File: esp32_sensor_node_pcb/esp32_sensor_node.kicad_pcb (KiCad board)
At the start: 4 copper layers, 49.9 x 59.9 mm, 28 parts, among them J1 Conn_02x10_Odd_Even, Q1 2N7002K, SW1 SW_DIP_x01, U1 HT7833, U2 ESP32-WROOM-E, U3 MAX3483AEASA+

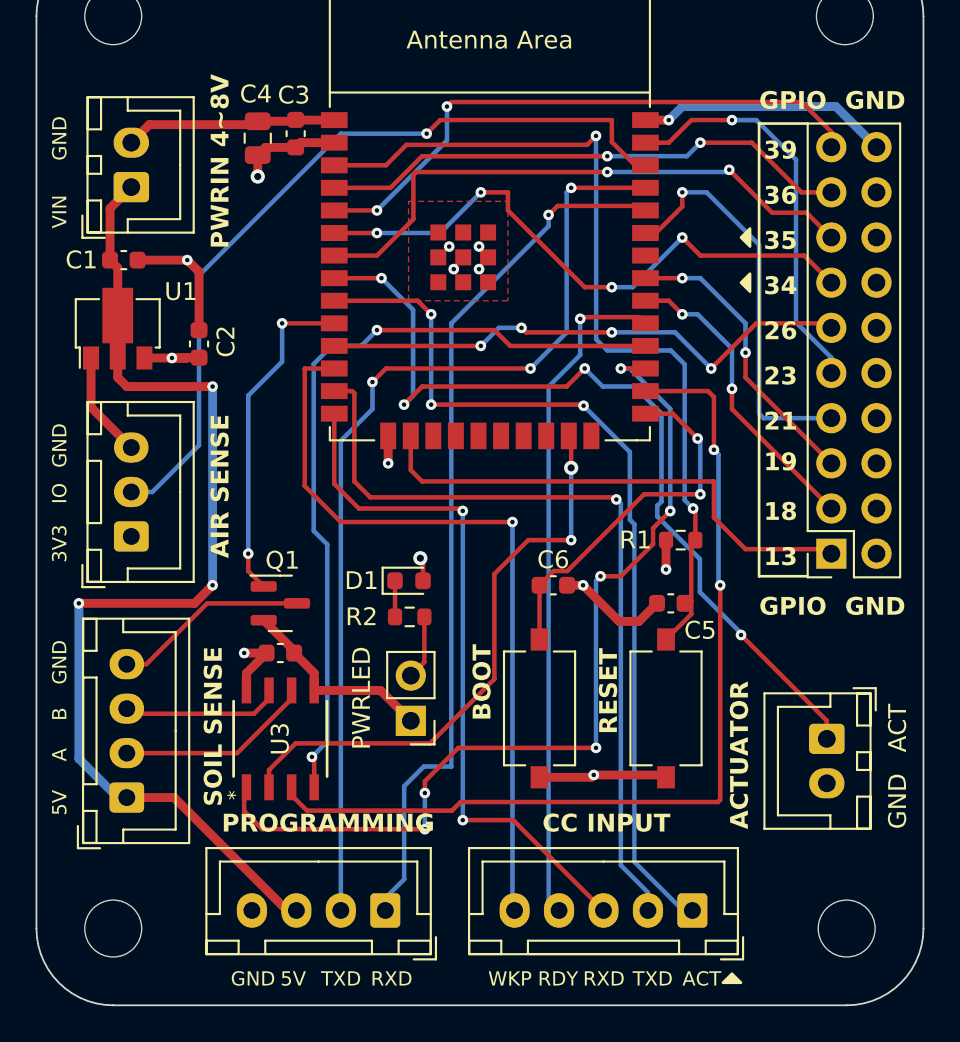
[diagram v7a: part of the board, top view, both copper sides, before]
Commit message: Added constraints to board setup according to JLCPCB specifications for DRC checker. Arranged some text on silkscreen and some routing.
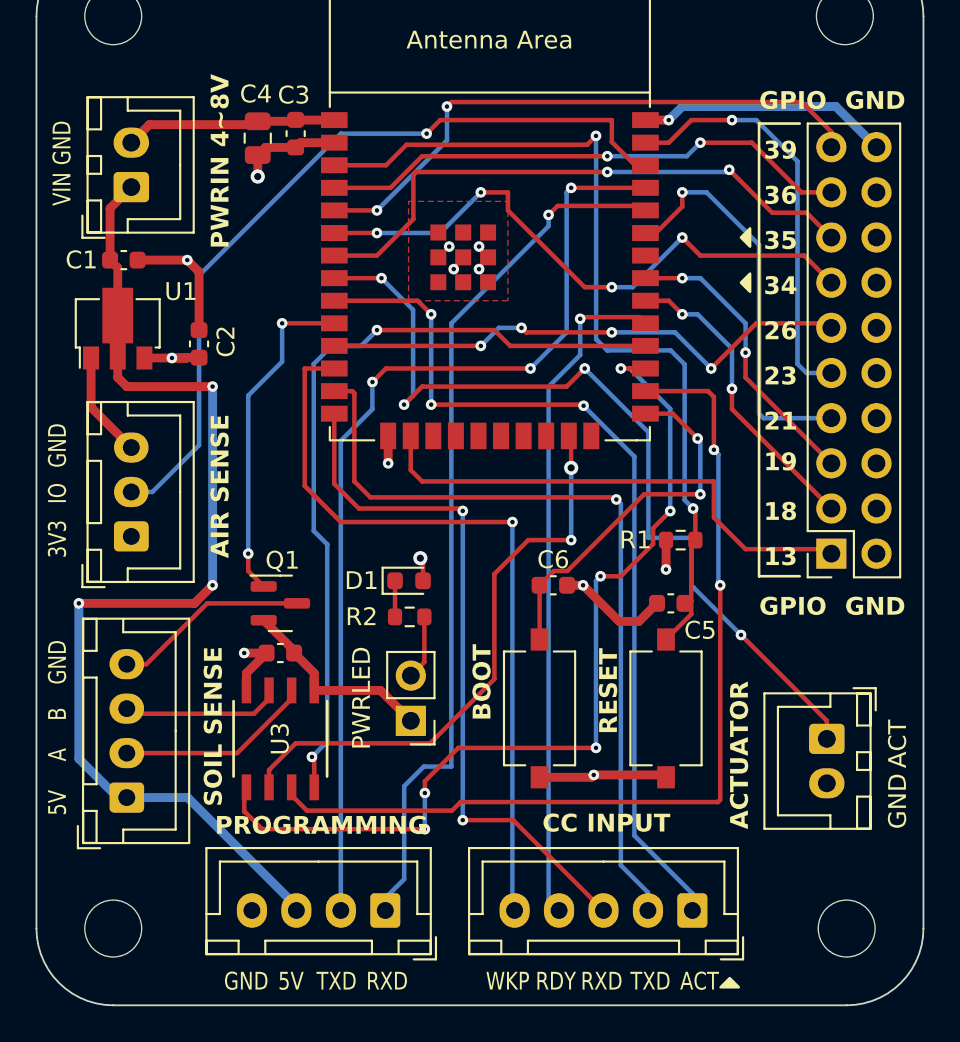
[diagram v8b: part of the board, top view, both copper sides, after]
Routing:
- net GPIO23: track 22.7 -> 23.6 mm
- net +5V: track 59.5 -> 60.2 mm
